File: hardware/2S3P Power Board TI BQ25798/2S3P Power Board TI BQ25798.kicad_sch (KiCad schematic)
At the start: 15 parts, among them U101 BQ25798RQMR

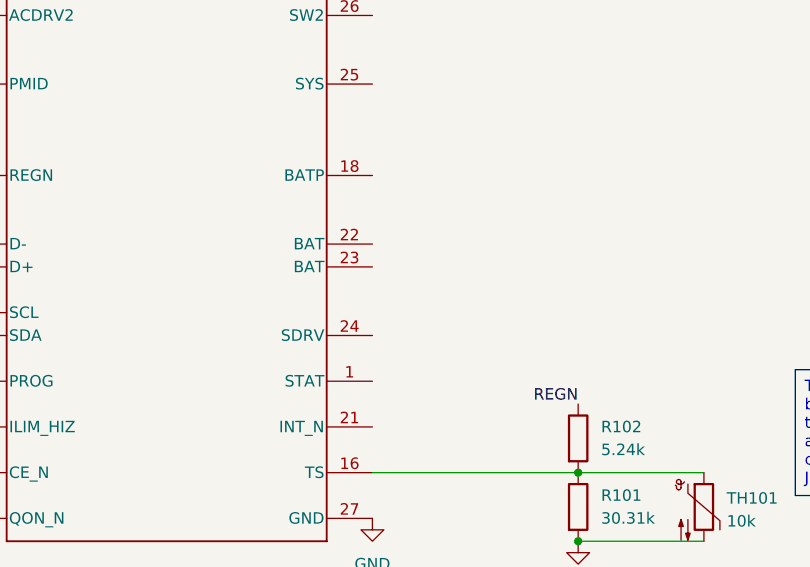
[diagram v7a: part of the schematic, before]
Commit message: Checkpointing work on configuring the BQ25798
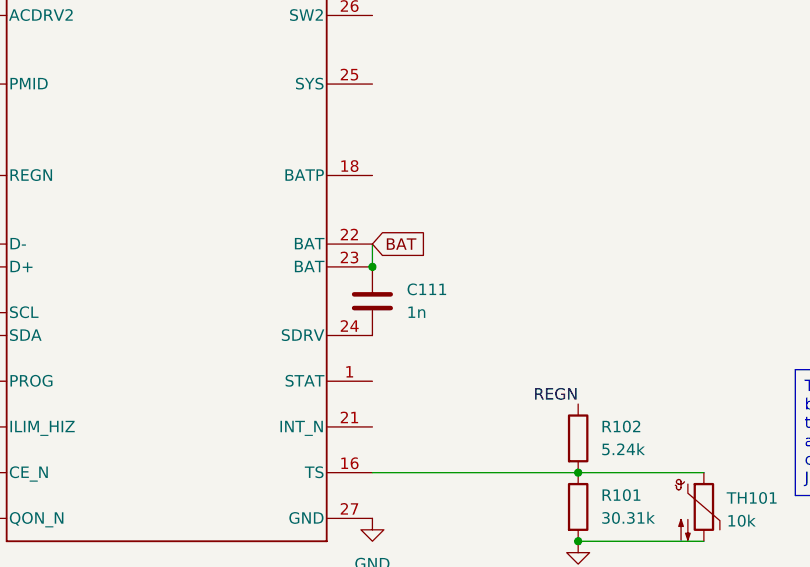
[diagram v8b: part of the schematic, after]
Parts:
- added C111: 1n, Capacitor_SMD:C_0402_1005Metric, symbol Device:C
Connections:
- net BAT: now reaches U101.22 (BAT)
- net BAT: now also U101.23 (BAT), C111.1
- net at U101.24 (SDRV): now also C111.2
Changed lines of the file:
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@@
   (junction (at 49.53 58.42) (diameter 0) (color 0 0 0 0)
+  )
+  (junction (at 165.1 109.22) (diameter 0) (color 0 0 0 0)
   )
   (junction (at 62.23 88.9) (diameter 0) (color 0 0 0 0)
@@
     (stroke (width 0) (type default))
   )
+  (wire (pts (xy 165.1 106.68) (xy 165.1 109.22))
+    (stroke (width 0) (type default))
+  )
   (wire (pts (xy 88.9 121.92) (xy 119.38 121.92))
     (stroke (width 0) (type default))
@@
     )
   )
+  (global_label "BAT" (shape input) (at 165.1 106.68 0) (fields_autoplaced)
+    (effects (font (size 1.27 1.27)) (justify left))
+    (property "Intersheetrefs" "${INTERSHEET_REFS}" (at 171.4114 106.68 0)
+      (effects (font (size 1.27 1.27)) (justify left) hide)
+    )
+  )
   (global_label "POWER_SDA" (shape input) (at 119.38 116.84 180) (fields_autoplaced)
     (effects (font (size 1.27 1.27)) (justify right))
@@
         )
       )
+    )
+  )
+  (symbol (lib_id "Device:C") (at 165.1 113.03 0) (unit 1)
+    (in_bom yes) (on_board yes) (dnp no) (fields_autoplaced)
+    (property "Reference" "C111" (at 168.91 111.76 0)
+      (effects (font (size 1.27 1.27)) (justify left))
+    )
+    (property "Value" "1n" (at 168.91 114.3 0)
+      (effects (font (size 1.27 1.27)) (justify left))
+    )
+    (property "Footprint" "Capacitor_SMD:C_0402_1005Metric" (at 166.0652 116.84 0)
+      (effects (font (size 1.27 1.27)) hide)
+    )
+    (property "Datasheet" "~" (at 165.1 113.03 0)
+      (effects (font (size 1.27 1.27)) hide)
+    )
+    (property "MPN" "C76947" (at 165.1 113.03 0)
+      (effects (font (size 1.27 1.27)) hide)
+    )
+    (property "Manufacturer" "Murata Electronics" (at 165.1 113.03 0)
+      (effects (font (size 1.27 1.27)) hide)
+    )
+    (property "Manufacturer Part Number" "GRM1555C1H102JA01D" (at 165.1 113.03 0)
+      (effects (font (size 1.27 1.27)) hide)
+    )
+    (pin "1")
+    (pin "2")
+    (instances
+      (project "2S3P Power Board TI BQ25798"
+        (path "/d7fbba2e-84c5-4e09-9d36-52dae726d12d"
+          (reference "C111") (unit 1)
+        )
+      )
